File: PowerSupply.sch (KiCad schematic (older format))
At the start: 27 parts, among them J7 USB_B_Micro, U1 LPC54616J512, U11 MP1582, U6 TLV70233_SOT23-5

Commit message: Fix few bugs, review design
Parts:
- D1: footprint Package_TO_SOT_SMD:SOT-143 -> Package_TO_SOT_SMD:SOT-143_Handsoldering
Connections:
- net GND: now also D5.2 (A); no longer D5.1 (K)
- net at C45.1, L8.1, U11.1 (SW): now also D5.1 (K); no longer D5.2 (A)
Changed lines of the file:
@@
 encoding utf-8
 Sheet 5 6
-Title ""
-Date ""
-Rev ""
-Comp ""
+Title "CANBOX LPC546xx - Power"
+Date "2019-06-02"
+Rev "1"
+Comp "Thorsten Wilmer"
 Comment1 ""
 Comment2 ""
@@
 F 0 "D1" H 5694 2246 50  0000 L CNN
 F 1 "PRTR5V0U2X" H 5694 2155 50  0000 L CNN
-F 2 "Package_TO_SOT_SMD:SOT-143" H 5210 2200 50  0001 C CNN
+F 2 "Package_TO_SOT_SMD:SOT-143_Handsoldering" H 5210 2200 50  0001 C CNN
 F 3 "https://assets.nexperia.com/documents/data-sheet/PRTR5V0U2X.pdf" H 5210 2200 50  0001 C CNN
 F 4 "PRTR5V0U2X,215" H 5150 2200 50  0001 C CNN "OP"
@@
 F 6 "B340AE-13" H 0   0   50  0001 C CNN "DigiKez"
 	1    5650 3600
-	0    -1   -1   0
+	0    1    1    0
 $EndComp
 Wire Wire Line
@@
 Wire Wire Line
 	5150 3450 5300 3450
-Connection ~ 5650 3450
 $Comp
 L canbox-rescue:R-Device R30
@@
 	7250 4350 7250 3950
 Connection ~ 6700 4350
+Connection ~ 5650 3450
 $EndSCHEMATC

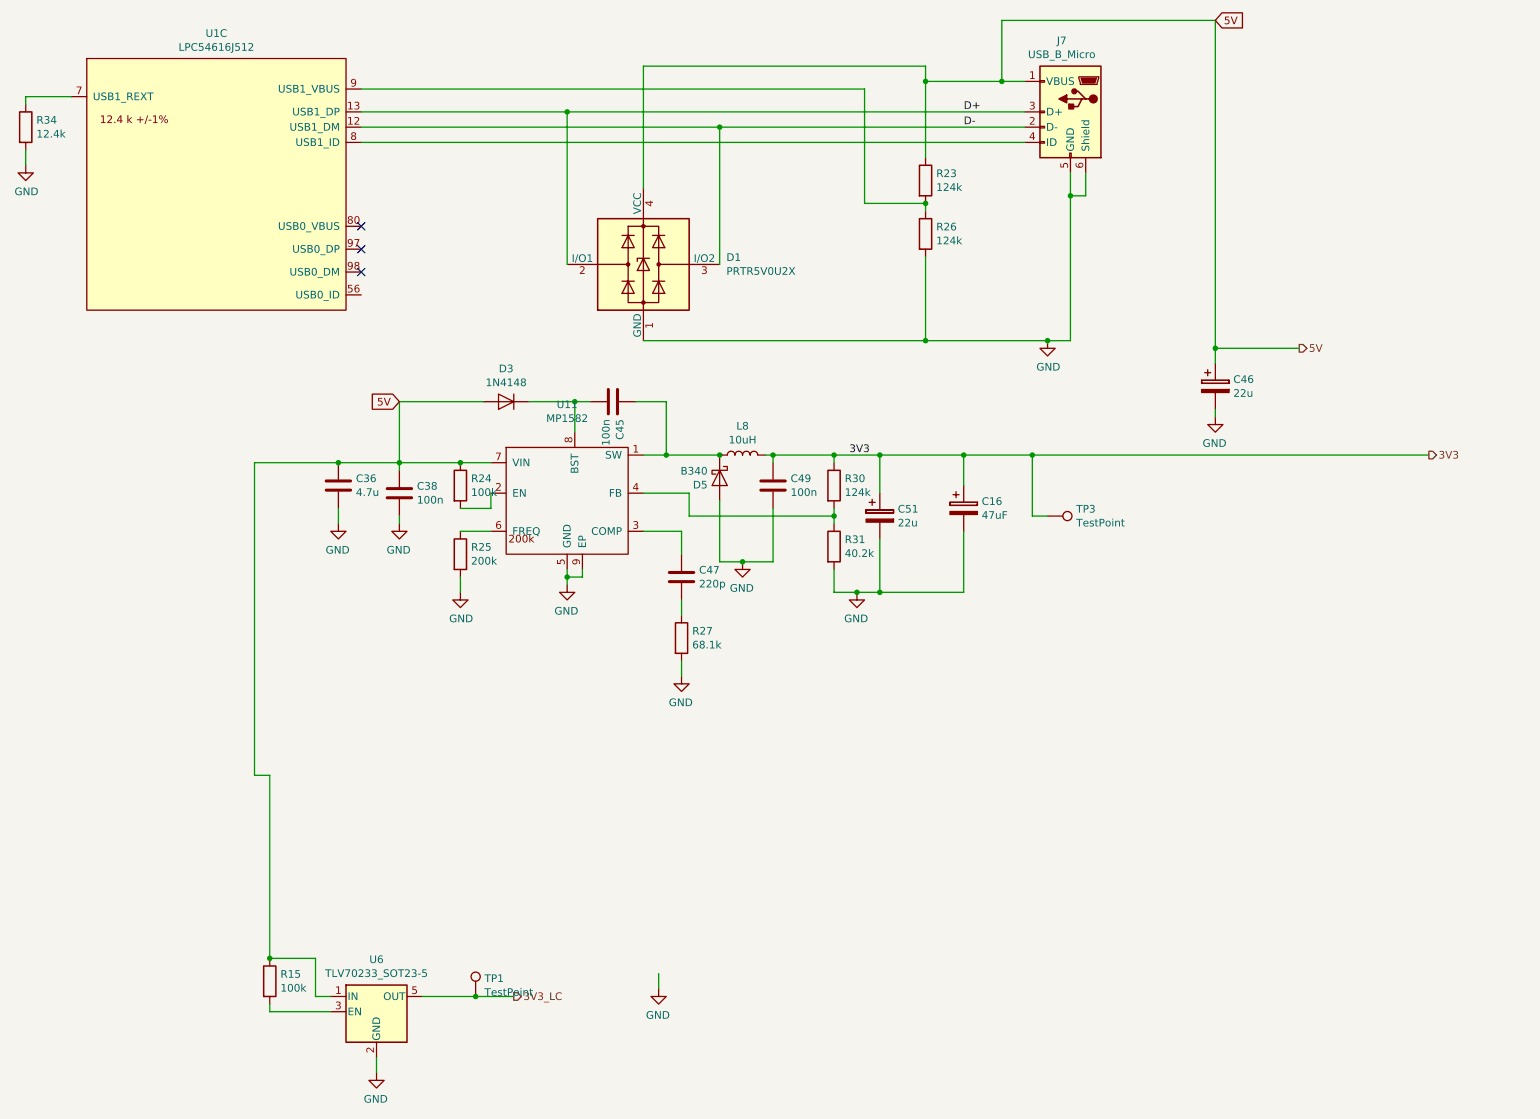
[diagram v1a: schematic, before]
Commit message: V3 bigger board, RMII instrumentation, inverter
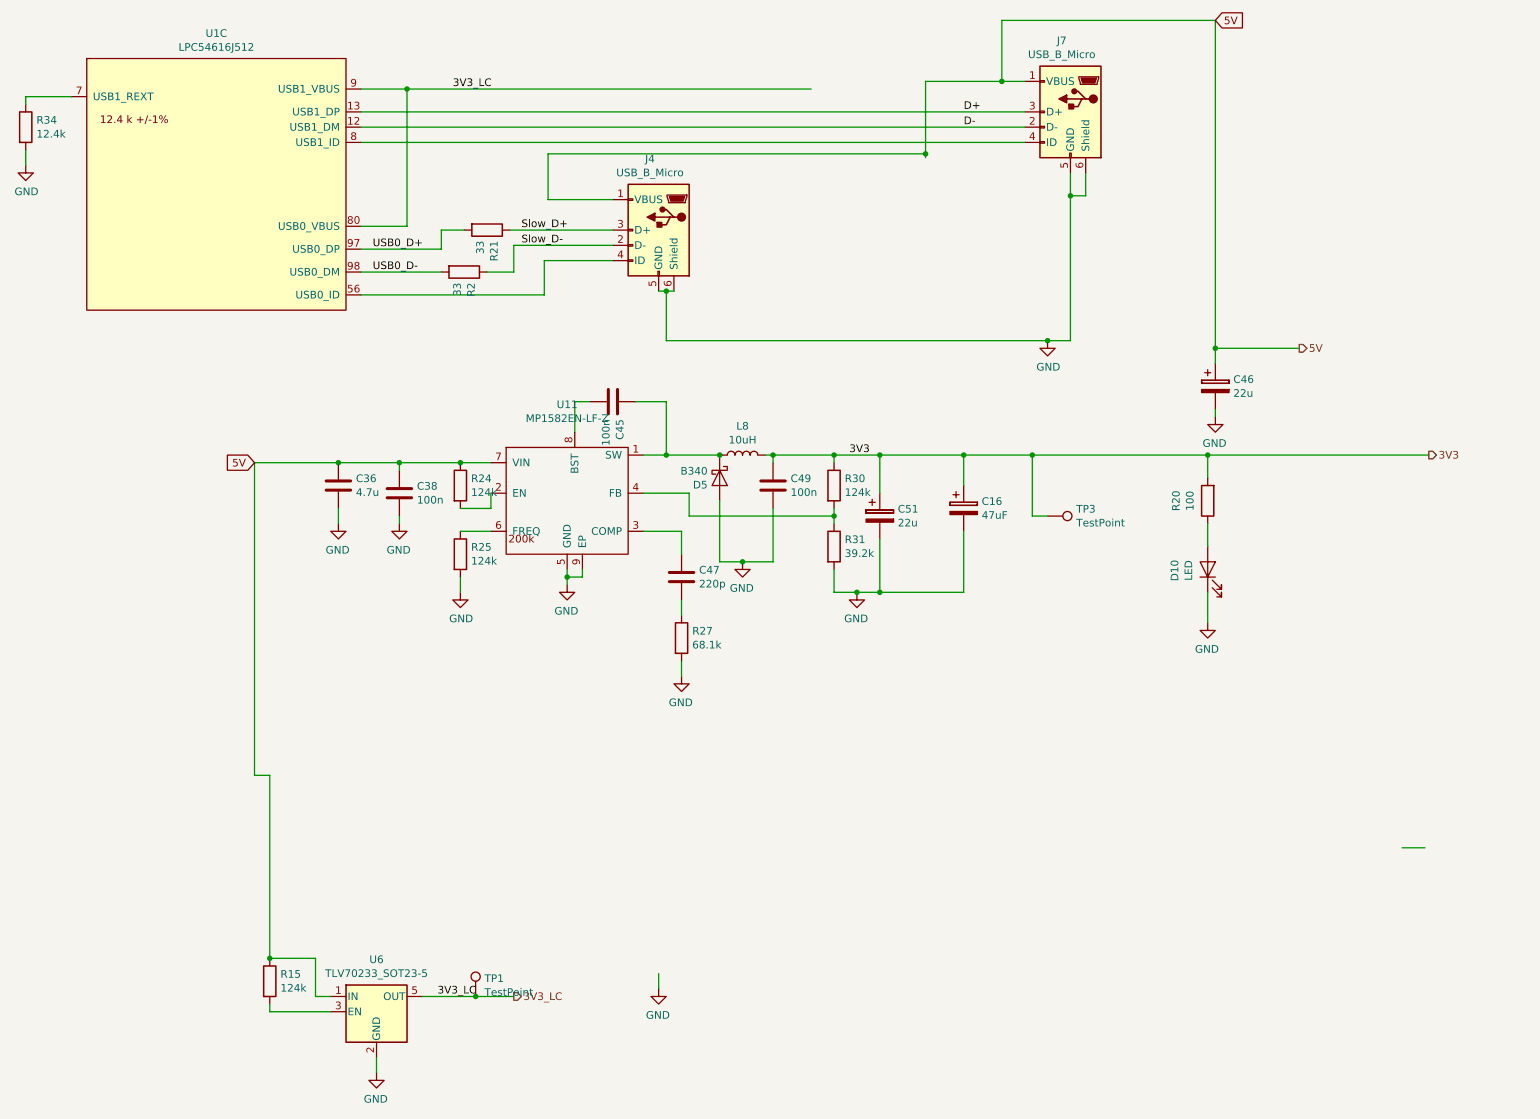
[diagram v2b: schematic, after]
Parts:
- removed D1: PRTR5V0U2X, Package_TO_SOT_SMD:SOT-143_Handsoldering, symbol canbox-rescue:PRTR5V0U2X-Power_Protection
- removed D3: 1N4148, Diode_THT:D_DO-35_SOD27_P7.62mm_Horizontal, symbol canbox-rescue:1N4148-Diode
- removed R23, R26: 124k, Resistor_SMD:R_0805_2012Metric_Pad1.15x1.40mm_HandSolder, symbol canbox-rescue:R-Device
- added D10: LED, LED_SMD:LED_1210_3225Metric, symbol canbox-rescue:LED-Device
- added J4: USB_B_Micro, cypress:MicroUsb, symbol canbox-rescue:USB_B_Micro-Connector
- added R2, R21: 33, Resistor_SMD:R_0805_2012Metric_Pad1.15x1.40mm_HandSolder, symbol canbox-rescue:R-Device
- added R20: 100, Resistor_SMD:R_0805_2012Metric_Pad1.15x1.40mm_HandSolder, symbol canbox-rescue:R-Device
- C16: JLC (none) -> C45783; OP (none) -> CL21A226MAQNNNE
- C36: JLC (none) -> C1779; OP CL21A475KOFNNNG -> CL21A475KAQNNNE
- C38, C45, C49: JLC (none) -> C49678; OP C0805C103K1RACTU -> CC0805KRX7R9BB104
- C46, C51: JLC (none) -> C45783
- C47: JLC (none) -> C53172
- D5: footprint Diode_SMD:D_SMC -> Diode_SMD:D_SMB-SMC_Universal_Handsoldering; JLC (none) -> C22452
- L8: JLC (none) -> C139506; OP ECS-MPIL0630-100MC -> SWRB1204S-100MT
- R15, R24: value 100k -> 124k; JLC (none) -> C17407; OP CR0805-JW-104ELFCT-ND -> 0805W8F1003T5E
- R25: value 200k -> 124k; JLC (none) -> C17539; OP RMCF0805JT200K -> 0805W8F2003T5E
- R27: JLC (none) -> C17795; OP ERJ-6ENF6812V -> 0805W8F6812T5E
- R30: JLC (none) -> C17440; OP RMCF0805FT124K -> 0805W8F1243T5E
- R31: value 40.2k -> 39.2k; JLC (none) -> C17678; OP ERJ-6ENF4022V -> 0805W8F4022T5E
- R34: JLC (none) -> C30908; OP RMCF0805FT12K4 -> 0805W8F1242T5E
- U11: value MP1582 -> MP1582EN-LF-Z; JLC (none) -> C15051
- U6: JLC (none) -> C26833; OP (none) -> TLV70233DBVR
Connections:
- net labels added: Slow_D+, Slow_D-, USB0_D+, USB0_D-
- wire segments 101 -> 112
- no-connect marks 3 -> 0

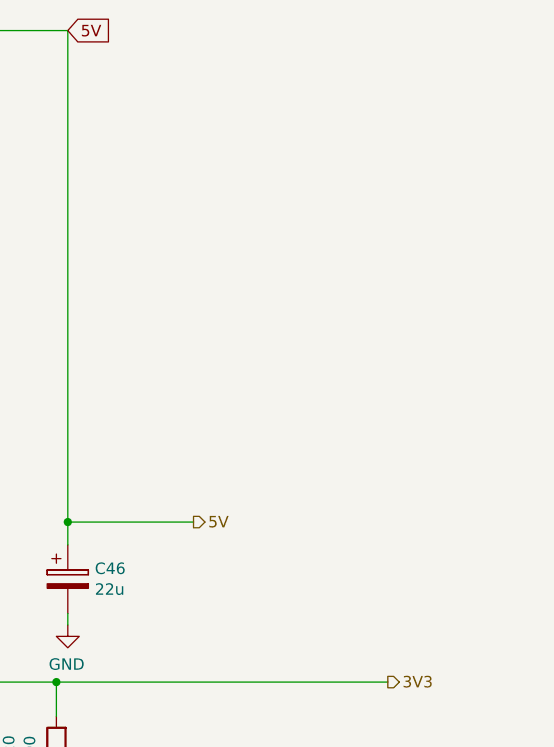
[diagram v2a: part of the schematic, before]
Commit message: Improve PCB, local loopback works - via RMII not
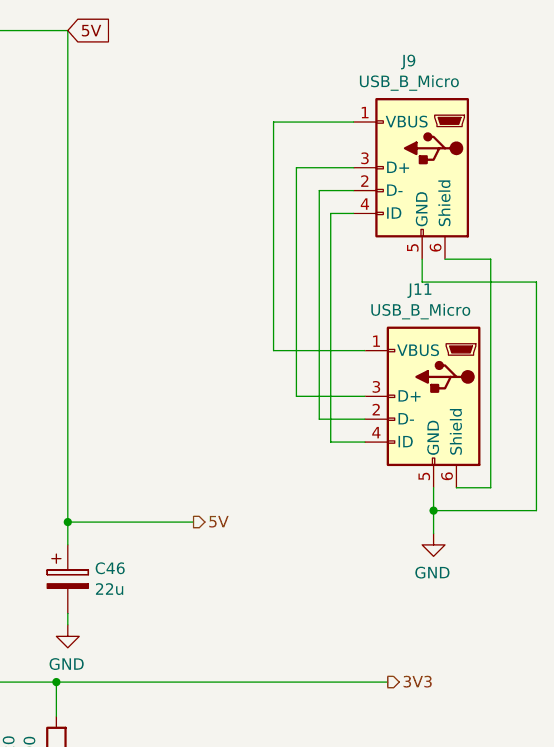
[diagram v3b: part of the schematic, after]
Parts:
- added J11, J9: USB_B_Micro, cypress:MicroUsb, symbol canbox-rescue:USB_B_Micro-Connector
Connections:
- wire segments 112 -> 133
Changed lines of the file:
@@
 Comment9 ""
 $EndDescr
-$Comp
-L canbox-rescue:USB_B_Micro-Connector J7
-U 1 1 5BDA6E1E
-P 7950 1200
-F 0 "J7" H 8007 1667 50  0000 C CNN
-F 1 "USB_B_Micro" H 8007 1576 50  0000 C CNN
-F 2 "cypress:MicroUsb" H 8100 1150 50  0001 C CNN
-F 3 "~" H 8100 1150 50  0001 C CNN
-F 4 "1050170001" H 7950 1200 50  0001 C CNN "OP"
-F 5 "ali" H 0   0   50  0001 C CNN "notes"
-	1    7950 1200
-	-1   0    0    -1
-$EndComp
 Wire Wire Line
 	3550 3550 3550 3500
@@
 Text Label 3900 1050 0    50   ~ 0
 3V3_LC
+$Comp
+L canbox-rescue:USB_B_Micro-Connector J7
+U 1 1 5BDA6E1E
+P 7950 1200
+F 0 "J7" H 8007 1667 50  0000 C CNN
+F 1 "USB_B_Micro" H 8007 1576 50  0000 C CNN
+F 2 "cypress:MicroUsb" H 8100 1150 50  0001 C CNN
+F 3 "~" H 8100 1150 50  0001 C CNN
+F 4 "1050170001" H 7950 1200 50  0001 C CNN "OP"
+F 5 "ali" H 0   0   50  0001 C CNN "notes"
+	1    7950 1200
+	-1   0    0    -1
+$EndComp
+$Comp
+L canbox-rescue:USB_B_Micro-Connector J9
+U 1 1 5E3C43EB
+P 10450 1200
+F 0 "J9" H 10507 1667 50  0000 C CNN
+F 1 "USB_B_Micro" H 10507 1576 50  0000 C CNN
+F 2 "cypress:MicroUsb" H 10600 1150 50  0001 C CNN
+F 3 "~" H 10600 1150 50  0001 C CNN
+F 4 "1050170001" H 10450 1200 50  0001 C CNN "OP"
+F 5 "ali" H 2500 0   50  0001 C CNN "notes"
+	1    10450 1200
+	-1   0    0    -1
+$EndComp
+$Comp
+L canbox-rescue:USB_B_Micro-Connector J11
+U 1 1 5E3D3C08
+P 10500 2200
+F 0 "J11" H 10557 2667 50  0000 C CNN
+F 1 "USB_B_Micro" H 10557 2576 50  0000 C CNN
+F 2 "cypress:MicroUsb" H 10650 2150 50  0001 C CNN
+F 3 "~" H 10650 2150 50  0001 C CNN
+F 4 "1050170001" H 10500 2200 50  0001 C CNN "OP"
+F 5 "ali" H 2550 1000 50  0001 C CNN "notes"
+	1    10500 2200
+	-1   0    0    -1
+$EndComp
+Wire Wire Line
+	10150 1000 9800 1000
+Wire Wire Line
+	9800 1000 9800 2000
+Wire Wire Line
+	9800 2000 10200 2000
+Wire Wire Line
+	10200 2200 9900 2200
+Wire Wire Line
+	9900 2200 9900 1200
+Wire Wire Line
+	9900 1200 10150 1200
+Wire Wire Line
+	10150 1300 10000 1300
+Wire Wire Line
+	10000 1300 10000 2300
+Wire Wire Line
+	10000 2300 10200 2300
+Wire Wire Line
+	10200 2400 10050 2400
+Wire Wire Line
+	10050 2400 10050 1400
+Wire Wire Line
+	10050 1400 10150 1400
+$Comp
+L canbox-rescue:GND-power #PWR0109
+U 1 1 5E3DA6CD
+P 10500 2800
+F 0 "#PWR0109" H 10500 2550 50  0001 C CNN
+F 1 "GND" H 10505 2627 50  0000 C CNN
+F 2 "" H 10500 2800 50  0001 C CNN
+F 3 "" H 10500 2800 50  0001 C CNN
+	1    10500 2800
+	-1   0    0    -1
+$EndComp
+Wire Wire Line
+	10500 2800 10500 2700
+Wire Wire Line
+	10950 2700 10950 1700
+Wire Wire Line
+	10950 1700 10450 1700
+Wire Wire Line
+	10450 1700 10450 1600
+Wire Wire Line
+	10500 2700 10950 2700
+Connection ~ 10500 2700
+Wire Wire Line
+	10500 2700 10500 2600
+Wire Wire Line
+	10550 1600 10750 1600
+Wire Wire Line
+	10750 1600 10750 2600
+Wire Wire Line
+	10750 2600 10600 2600
 $EndSCHEMATC
